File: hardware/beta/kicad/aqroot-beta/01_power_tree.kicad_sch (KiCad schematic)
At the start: 49 parts, among them J3 USB_C_Receptacle_USB2.0_16P, J4 JST-PH-2 BATTERY, SW9 SW_SPST, U10 USBLC6-2SC6, U11 BQ25185, U12 TPS63020, U13 TPS61023, U14 MAX17048

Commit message: AQROOT Beta: add documented power-tree test points
Three test points required by the repo documentation existed on paper only.

  TP13  TPS63020 EN       Net-(SW9-B)          05 Decisions Log:980
                                               'EN test point present'
  TP14  TPS63020 PS/SYNC  Net-(U12-PS_SYNC)    kicad README:474
  TP15  MAX17048 CELL     /BAT_PROTECTED_P     05 Decisions Log:406
                                               'Test point: TP_FG_CELL'

All three use Connector:TestPoint with TestPoint:TestPoint_Pad_D1.0mm,
matching TP6-TP12, and follow the existing style (body/marker above the pin,
wire leaving downward or sideways so the marker never sits on its own wire).

Connection method per net:
  TP13 vertical wire down to a T-junction on the EN wire
       (190.5,69.85)-(228.6,69.85)
  TP14 L-route: horizontal then vertical up to a T-junction on
       (213.36,72.39)-(228.6,72.39). A straight drop was rejected because
       its corridor crossed the EN wire at y=69.85 - a stray junction there
       would have shorted EN to PS/SYNC.
  TP15 joins by a BAT_PROTECTED_P local label, the same way the other five
       labels already distribute that net across the sheet. The U14 wire
       cluster is only ~4 mm wide with no interior grid point to T into.

All coordinates on the 1.27 mm grid; every placement was checked for
clearance around the marker/labels and along the wire corridor before
writing. PS/SYNC keeps R42 0R to GND - only a test point was added, since
the documentation offers 'test point / solder-jumper / DNP option' as
alternatives and does not make a jumper mandatory.

Verified with kicad-cli: each TP adds exactly one node to its intended net
and no pre-existing pin changed net. BAT_CONNECTOR_P {J4.1} unchanged and
still distinct from BAT_PROTECTED_P; the parked reverse-polarity boundary is
untouched. ERC unchanged: raw 48, unique 24, excluded 24, real 0.

Co-Authored-By: Claude Opus 5 <noreply@anthropic.com>
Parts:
- added TP13, TP14, TP15: TestPoint, TestPoint:TestPoint_Pad_D1.0mm, symbol Connector:TestPoint
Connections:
- net BAT_PROTECTED_P: now also TP15.1
- net at R42.2, U12.13 (PS_SYNC): now also TP14.1
- net at R43.1, SW9.2 (B), U12.12 (EN): now also TP13.1

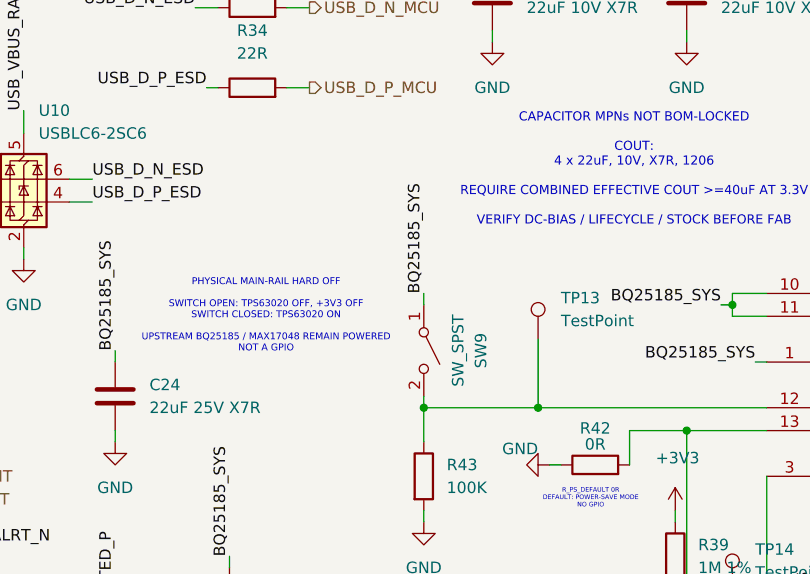
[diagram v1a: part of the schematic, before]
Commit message: AQROOT Beta: add TPS63020 enable bypass DNP option
R_EN_BYPASS was specified in the docs but absent from the schematic.

Endpoints are unambiguous in the repo:
  05 Decisions Log 'The superseded 0R link': R_EN_LINK = 0R (VINA->EN) is
  withdrawn and 'survives only as R_EN_BYPASS = 0R, DNP - VINA -> EN, bench
  bypass only if the physical switch is unavailable.'
  01 Hardware Core repeats it: 'surviving only as R_EN_BYPASS 0R DNP
  (never firmware-driven)'.

Resolved against the schematic: TPS63020 VINA is U12 pin 1 on
/BQ25185_SYS; EN is U12 pin 12 on Net-(SW9-B). So the part sits exactly in
parallel with the SPST hard-off switch SW9, which spans the same two nets.

Added R68 = 0R, dnp yes, Resistor_SMD:R_0603_1608Metric, placed vertically
in clear space left of SW9. VINA side joins /BQ25185_SYS by a local label
(the net is already named by 10+ labels); EN side is wired to the EN wire
with a junction, since Net-(SW9-B) is unnamed and must be joined
physically. Reference R68 is the next free designator; value string
'0R DNP' matches the existing DNP convention (C21/C22 '100pF DNP',
R49/R50 '4.7k DNP').

Hard-off behaviour is preserved: the part is flagged dnp=yes, so it is not
fitted and provides no VINA->EN path on an assembled board. With SW9 open,
EN is still pulled low by the 100k R_EN_PULLDOWN. The documented warning
stands - do not populate R68 while the hard-off switch is fitted.

Verified with kicad-cli: R68.1 and SW9.1 share /BQ25185_SYS, R68.2 and
SW9.2 share Net-(SW9-B) - genuinely parallel. No pre-existing pin changed
net. ERC unchanged: raw 48, unique 24, excluded 24, real 0.

Co-Authored-By: Claude Opus 5 <noreply@anthropic.com>
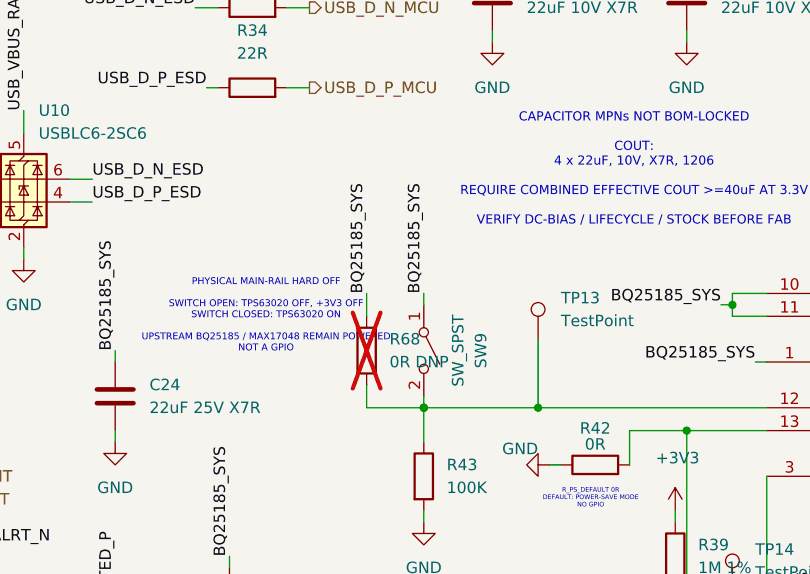
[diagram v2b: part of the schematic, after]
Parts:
- added R68: 0R DNP, Resistor_SMD:R_0603_1608Metric, symbol Device:R
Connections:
- net BQ25185_SYS: now also R68.1
- net at R43.1, SW9.2 (B), TP13.1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: now also R68.2
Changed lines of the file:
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@@
+	)
+	(junction
+		(at 190.5 69.85)
+		(diameter 0)
+		(color 0 0 0 0)
 	)
 	(junction
@@
 	(wire
 		(pts
+			(xy 184.15 59.69) (xy 184.15 57.15)
+		)
+		(stroke
+			(width 0)
+			(type default)
+		)
+	)
+	(wire
+		(pts
+			(xy 184.15 67.31) (xy 184.15 69.85)
+		)
+		(stroke
+			(width 0)
+			(type default)
+		)
+	)
+	(wire
+		(pts
+			(xy 184.15 69.85) (xy 190.5 69.85)
+		)
+		(stroke
+			(width 0)
+			(type default)
+		)
+	)
+	(wire
+		(pts
 			(xy 203.2 62.23) (xy 203.2 69.85)
 		)
@@
 			(width 0)
 			(type default)
+		)
+	)
+	(label "BQ25185_SYS"
+		(at 184.15 57.15 90)
+		(effects
+			(font
+				(size 1.27 1.27)
+			)
+			(justify left bottom)
 		)
 	)
@@
 		)
 	)
+	(symbol
+		(lib_id "Device:R")
+		(at 184.15 63.5 0)
+		(unit 1)
+		(body_style 1)
+		(exclude_from_sim no)
+		(in_bom yes)
+		(on_board yes)
+		(in_pos_files yes)
+		(dnp yes)
+		(fields_autoplaced yes)
+		(property "Reference" "R68"
+			(at 186.69 62.2299 0)
+			(show_name no)
+			(do_not_autoplace no)
+			(effects
+				(font
+					(size 1.27 1.27)
+				)
+				(justify left)
+			)
+		)
+		(property "Value" "0R DNP"
+			(at 186.69 64.7699 0)
+			(show_name no)
+			(do_not_autoplace no)
+			(effects
+				(font
+					(size 1.27 1.27)
+				)
+				(justify left)
+			)
+		)
+		(property "Footprint" "Resistor_SMD:R_0603_1608Metric"
+			(at 182.372 63.5 90)
+			(hide yes)
+			(show_name no)
+			(do_not_autoplace no)
+			(effects
+				(font
+					(size 1.27 1.27)
+				)
+			)
+		)
+		(property "Datasheet" ""
+			(at 184.15 63.5 0)
+			(hide yes)
+			(show_name no)
+			(do_not_autoplace no)
+			(effects
+				(font
+					(size 1.27 1.27)
+				)
+			)
+		)
+		(property "Description" "Resistor"
+			(at 184.15 63.5 0)
+			(hide yes)
+			(show_name no)
+			(do_not_autoplace no)
+			(effects
+				(font
+					(size 1.27 1.27)
+				)
+			)
+		)
+		(pin "2"
+		)
+		(pin "1"
+		)
+		(instances
+			(project "aqroot-Beta"
+				(path "/8a0ad1ee-a49e-4cff-9a78-44823e373405/83b1880a-0a3b-496a-bce6-0dc4c72d8ece"
+					(reference "R68")
+					(unit 1)
+				)
+			)
+		)
+	)

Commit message: AQROOT Beta: lock BQ25185 package and assign verified DLH0010A footprint
MPN BQ25185DLHR and the DLH/WSON-10 package were already recorded in the
schematic symbol; the Markdown documentation was not. Both are now aligned,
and the footprint is assigned after geometric verification.

Footprint: Package_DFN_QFN:Texas_DLH0010A_WSON-10-1EP_2.2x2mm_P0.4mm_EP0.9x1.5mm

This stock footprint was accepted - unlike TPS63020/XFL4020, which have no
stock match - because it is not a generic WSON-10. It is TI's own DLH0010A
land pattern and the KiCad library cites the BQ25185 datasheet by URL in its
descr field: 'Texas DLH0010A WSON, 10 Pin (https://www.ti.com/lit/gpn/BQ25185)'.

Verified before assigning:
  package designator  DLH            -> Texas_DLH0010A          match
  signal pads         WSON-10        -> pads 1-10, 5 per side   match
  pitch               0.4 mm         -> 0.4 mm measured         match
  body                2.2 x 2.0 mm   -> F.Fab -1.1..1.1 x -1..1 match
  exposed pad         yes            -> pad 11, 0.9 x 1.5 mm    match
Symbol pins 1-10 + pin 11 (EP) map 1:1 onto pads 1-10 + pad 11 (EP) - the
EP numbering agrees, which is the usual WSON failure mode.

Applied to the symbol library, the lib_symbols cache and the U11 instance
together, verified identical in all three. The stale Package property text
('exact footprint still requires package-drawing verification') is replaced.

Not closed: TI's recommended-land-pattern section has not been read directly,
and thermal vias are excluded - a _ThermalVias variant exists and is a
layout/thermal decision for the power review, not a package decision.

Docs updated: 01 Hardware Core charger row, 06 BOM and Cost Tracker, and a
new dated section in 05 Design Decisions Log. That section also corrects the
previous audit's claim that BQ25185 had no MPN or package recorded - it did;
the audit had grepped only Markdown and filtered MPNs to parts that already
had footprints, so U11's was never shown.

Electrical circuit u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
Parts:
- U11: footprint (none) -> Package_DFN_QFN:Texas_DLH0010A_WSON-10-1EP_2.2x2mm_P0.4mm_EP0.9x1.5mm; Package 10-pin WSON DLH with exposed pad - exact footprint still re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 -> 10-pin WSON DLH (TI DLH0010A), 2.2 x 2.0 mm body, 0.4 mm pi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
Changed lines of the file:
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@@
 			)
 		)
-		(property "Footprint" ""
+		(property "Footprint" "Package_DFN_QFN:Texas_DLH0010A_WSON-10-1EP_2.2x2mm_P0.4mm_EP0.9x1.5mm"
 			(at 53.34 105.41 0)
 			(hide yes)
@@
 			)
 		)
-		(property "Package" "10-pin WSON DLH with exposed pad - exact footprint still requires package-drawing verification"
+		(property "Package" "10-pin WSON DLH (TI DLH0010A), 2.2 x 2.0 mm body, 0.4 mm pitch, exposed thermal pad; land pattern verified against TI DLH0010A - see 05 Design Decisions Log"
 			(at 53.34 105.41 0)
 			(hide yes)

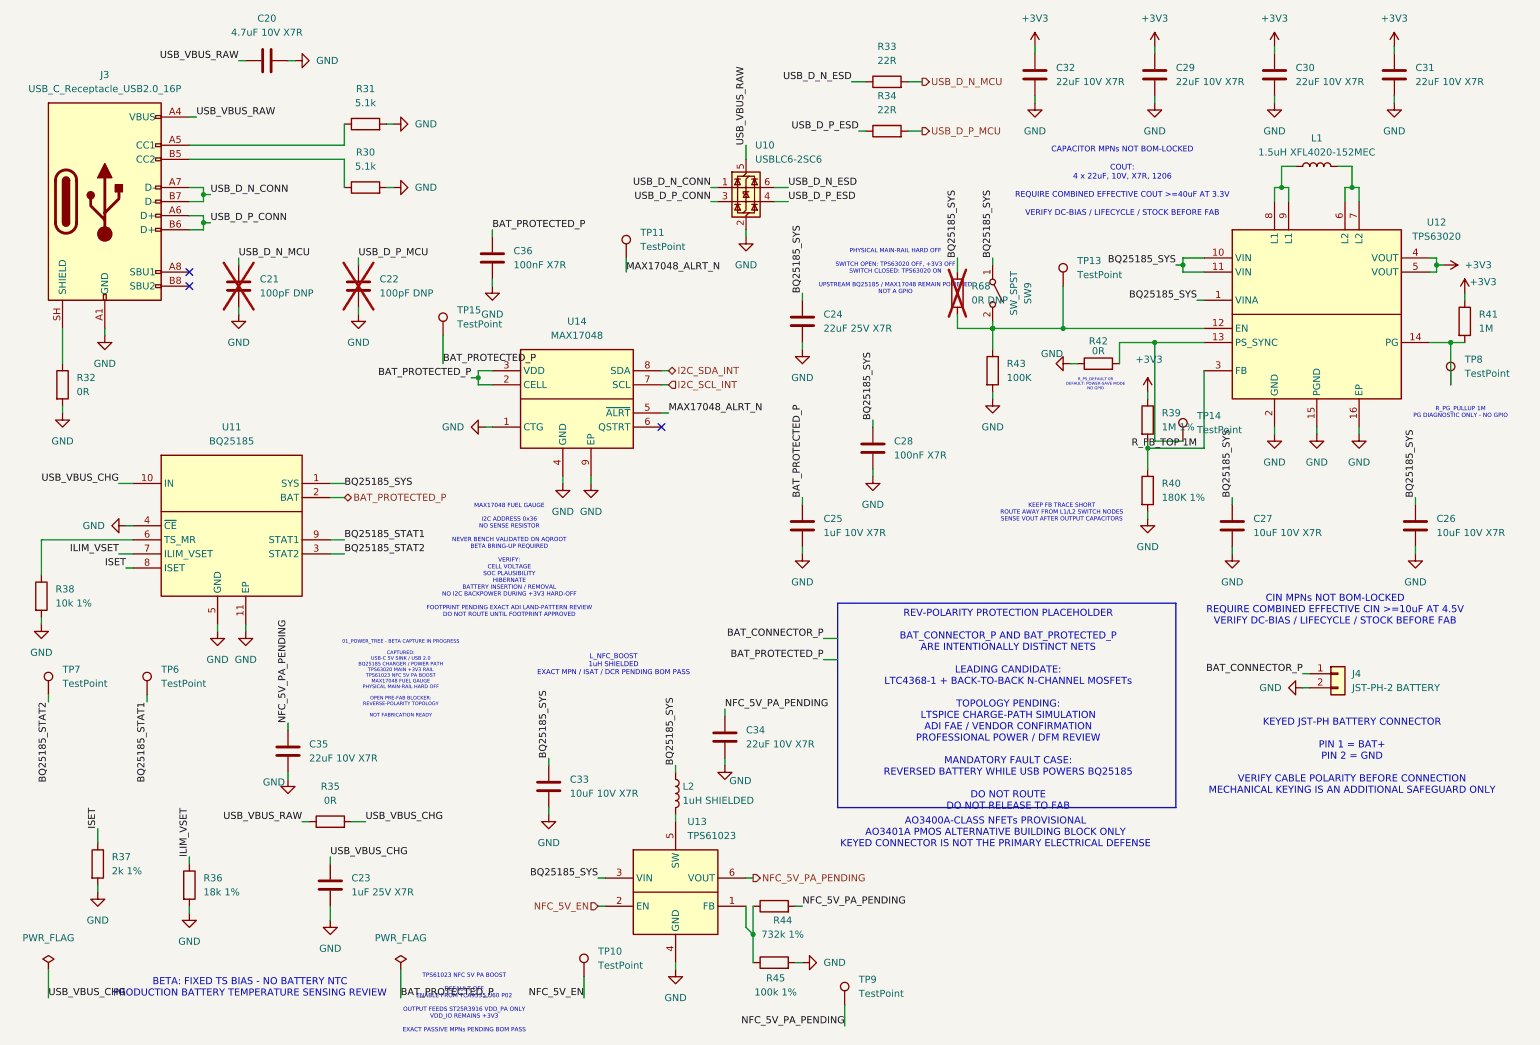
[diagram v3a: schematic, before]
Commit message: AQROOT Beta: lock resolved power and IR component metadata
Records exact MPN / manufacturer / package metadata for four parts whose
selection is now locked. Footprints deliberately left BLANK - locking a part
and verifying its land pattern are separate gates.

  L1   XFL4020-152MEC   Coilcraft                     1.5uH (was '1.5uH XFL4020-152MEC')
  L2   74438357010      Wurth Elektronik              1uH   (was '1uH SHIELDED')
  Q1   AO3400A          Alpha & Omega Semiconductor   AO3400A (was 'NMOS_TBD')
  U16  TCA9517ADGKR     Texas Instruments             TCA9517ADGK (value unchanged)

Instance-level properties only, on stock symbols (Device:L,
Transistor_FET:Q_NMOS_GSD, Logic_LevelTranslator:TCA9517ADGK) - no stock
library was edited and no project-local symbol was touched.

Deliberately NOT recorded, per the no-fabrication rule: Isat, DCR, current
ratings, body dimensions, Vds/Id/Rds(on). Each Note says to take those from
the manufacturer datasheet at BOM lock rather than from memory.

Q1 pin mapping cross-checked against the existing wiring: Q_NMOS_GSD gives
1 Gate / 2 Source / 3 Drain, and the schematic already has 1 -> IR_GATE,
2 -> GND, 3 -> IR_LED_K. Consistent, but the Note flags that AO3400A's real
pin order must be confirmed against the AOS datasheet before a footprint is
assigned. Topology and GPIO mapping unchanged.

L2's Note additionally records that its current rating still has to be
checked against the TI TPS61023 5V design calculation.

U12, U14 and U15 were inspected and already carried complete and correct
metadata - no change was needed. U12's apparent 16-pin/14-pin conflict is
explained by its own Note: pins 15 and 16 are KiCad-only logical numbers for
the unnumbered PGND pad and the exposed thermal pad, so it is a genuine
14-pin DSJ.

Verified with kicad-cli: netlist pin-to-net mapping byte-identical, ERC
unchanged raw 48 / unique 24 / excluded 24 / real 0.

Co-Authored-By: Claude Opus 5 <noreply@anthropic.com>
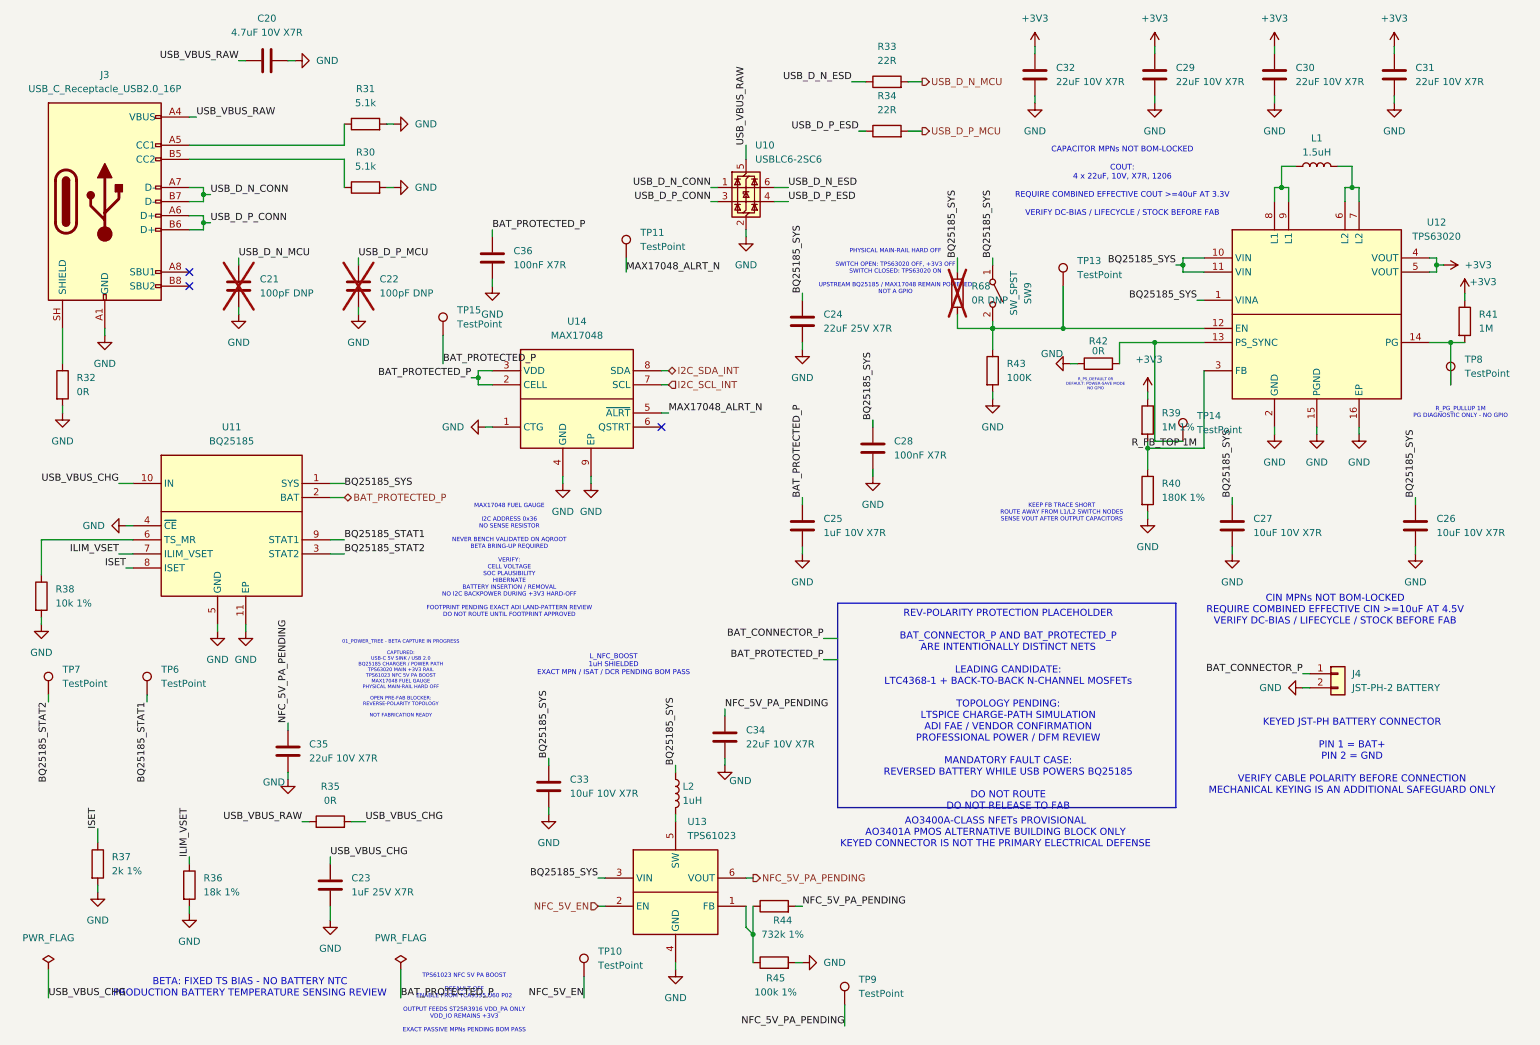
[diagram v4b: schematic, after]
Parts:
- L1: value 1.5uH XFL4020-152MEC -> 1.5uH; MPN (none) -> XFL4020-152MEC; Manufacturer (none) -> Coilcraft; Note (none) -> 1.5 uH +/-20%, LCSC C3033018. Isat/DCR/current rating NOT r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; Package (none) -> XFL4020 shielded moulded power inductor, 4.0 x 4.0 x 2.1 mm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
- L2: value 1uH SHIELDED -> 1uH; MPN (none) -> 74438357010; Manufacturer (none) -> Wurth Elektronik; Note (none) -> TPS61023 NFC 5V boost inductor (L_NFC_BOOST). Body size, DC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; Package (none) -> WE-LQS series shielded SMT power inductor - LOCKED. Footpri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
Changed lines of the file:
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@@
 			)
 		)
-		(property "Value" "1uH SHIELDED"
+		(property "Value" "1uH"
 			(at 134.62 154.9399 0)
 			(show_name no)
@@
 			)
 		)
+		(property "Note" "TPS61023 NFC 5V boost inductor (L_NFC_BOOST). Body size, DCR, Isat and current rating NOT recorded here - take them from the Wurth datasheet. Current rating must still be checked against the TI TPS61023 5V design calculation."
+			(at 133.35 153.67 0)
+			(hide yes)
+			(show_name no)
+			(do_not_autoplace no)
+			(effects
+				(font
+					(size 1.27 1.27)
+				)
+			)
+		)
+		(property "Package" "WE-LQS series shielded SMT power inductor - LOCKED. Footprint BLOCKED: needs the official Wurth recommended land pattern."
+			(at 133.35 153.67 0)
+			(hide yes)
+			(show_name no)
+			(do_not_autoplace no)
+			(effects
+				(font
+					(size 1.27 1.27)
+				)
+			)
+		)
+		(property "Manufacturer" "Wurth Elektronik"
+			(at 133.35 153.67 0)
+			(hide yes)
+			(show_name no)
+			(do_not_autoplace no)
+			(effects
+				(font
+					(size 1.27 1.27)
+				)
+			)
+		)
+		(property "MPN" "74438357010"
+			(at 133.35 153.67 0)
+			(hide yes)
+			(show_name no)
+			(do_not_autoplace no)
+			(effects
+				(font
+					(size 1.27 1.27)
+				)
+			)
+		)
 		(property "Description" "Inductor"
 			(at 133.35 153.67 0)
@@
 			)
 		)
-		(property "Value" "1.5uH XFL4020-152MEC"
+		(property "Value" "1.5uH"
 			(at 248.92 38.1 90)
 			(show_name no)
@@
 			(at 248.92 40.64 0)
 			(hide yes)
+			(show_name no)
+			(do_not_autoplace no)
+			(effects
+				(font
+					(size 1.27 1.27)
+				)
+			)
+		)
+		(property "Note" "1.5 uH +/-20%, LCSC C3033018. Isat/DCR/current rating NOT recorded here - take them from the Coilcraft datasheet at BOM lock rather than from memory."
+			(at 248.92 40.64 0)
+			(hide yes)
+			(show_name no)
+			(do_not_autoplace no)
+			(effects
+				(font
+					(size 1.27 1.27)
+				)
+			)
+		)
+		(property "Package" "XFL4020 shielded moulded power inductor, 4.0 x 4.0 x 2.1 mm max - LOCKED. Footprint BLOCKED: needs the official Coilcraft XFL4020 recommended land pattern; no stock KiCad XFL footprint exists."
+			(at 248.92 40.64 0)
+			(hide yes)
+			(show_name no)
+			(do_not_autoplace no)
+			(effects
+				(font
+					(size 1.27 1.27)
+				)
+			)
+		)
+		(property "Manufacturer" "Coilcraft"
+			(at 248.92 40.64 0)
+			(hide yes)
+			(show_name no)
+			(do_not_autoplace no)
+			(effects
+				(font
+					(size 1.27 1.27)
+				)
+			)
+		)
+		(property "MPN" "XFL4020-152MEC"
+			(at 248.92 40.64 0)
+			(hide yes)
